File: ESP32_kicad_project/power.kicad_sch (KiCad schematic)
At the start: 24 parts, among them J2 USB_C_Receptacle_USB2.0_16P, Q1 AO3401A, U1 TPS56339DDC

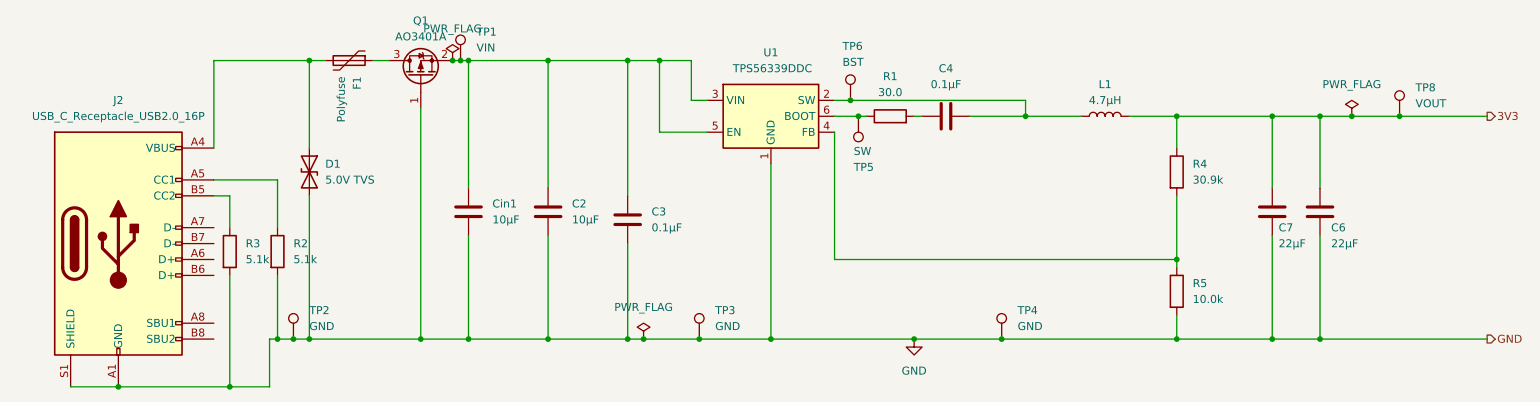
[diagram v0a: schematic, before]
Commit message: added USB chip, implemented ESP32 auto reset DTR RTS circuit
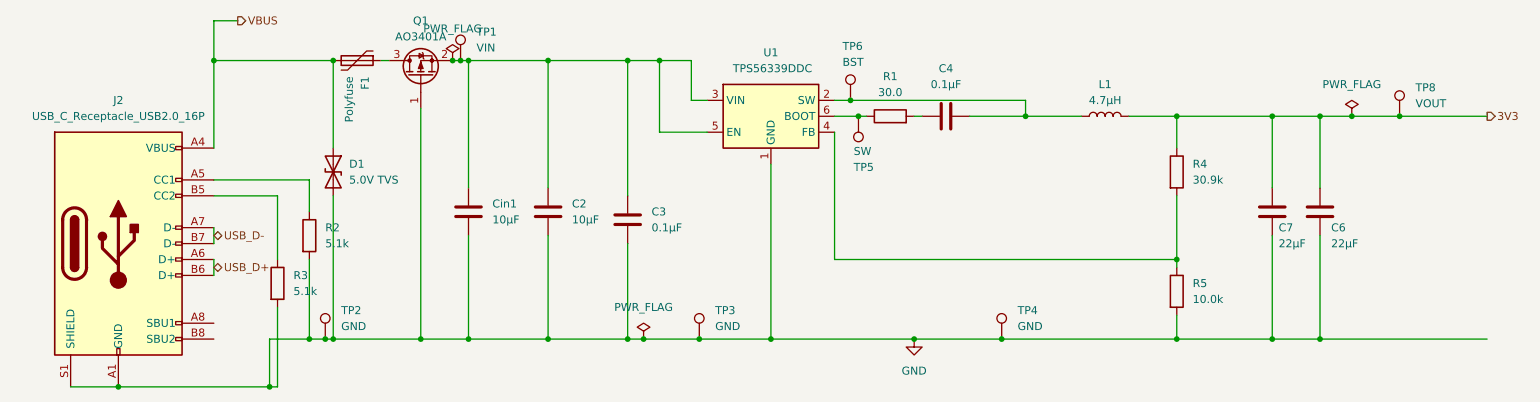
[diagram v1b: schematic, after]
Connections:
- net VBUS: now reaches D1.1 (A1), F1.2, J2.A4 (VBUS), J2.A9 (VBUS), J2.B4 (VBUS), J2.B9 (VBUS)
- net USB_D+: now reaches J2.A6 (D+)
- net USB_D+: now also J2.B6 (D+)
- net USB_D-: now reaches J2.A7 (D-)
- net USB_D-: now also J2.B7 (D-)
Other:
- moved on the sheet: D1, F1, R2, R3, TP2

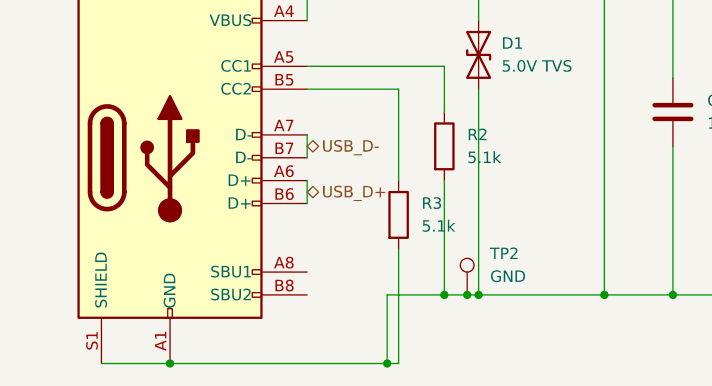
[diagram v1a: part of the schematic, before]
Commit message: completed USB-UART, created GPIO pin connectors, completed schematic work. moving on to PCB
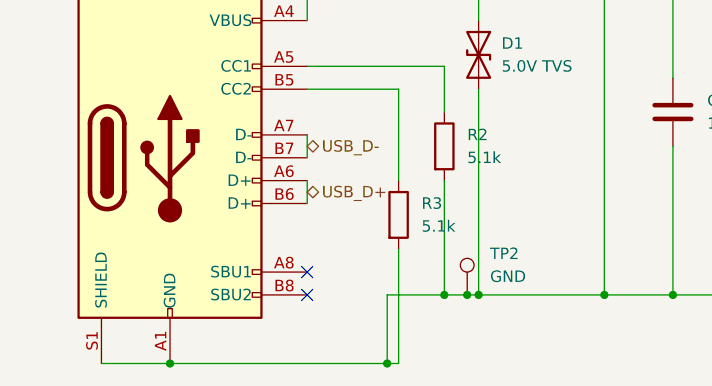
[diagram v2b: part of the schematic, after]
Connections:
- no-connect marks 0 -> 2
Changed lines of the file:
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@@
 		(color 0 0 0 0)
+	)
+	(no_connect
+		(at 58.42 118.11)
+	)
+	(no_connect
+		(at 58.42 115.57)
 	)
 	(wire

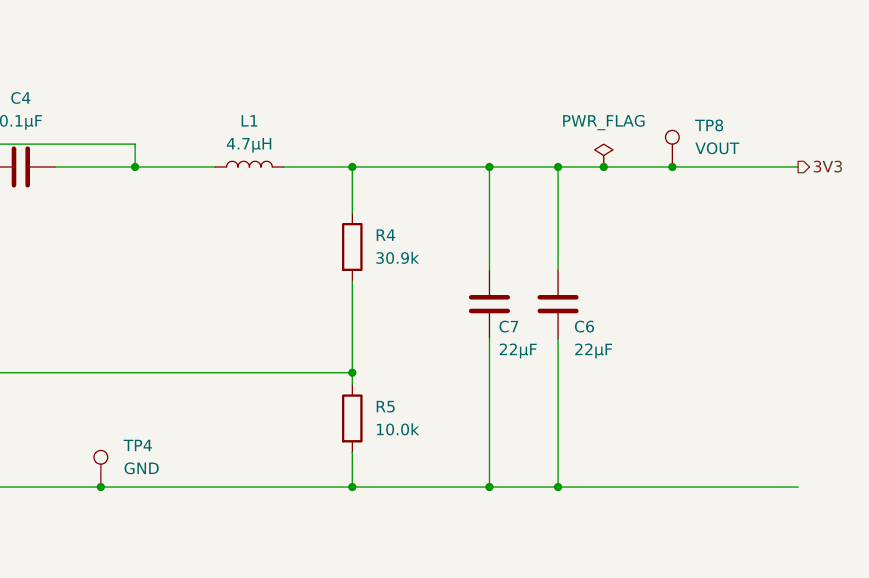
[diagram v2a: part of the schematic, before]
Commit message: completed schematic design, replaced regulator output inductor with a smaller part, fit components in a board in PCB editor, will start routing
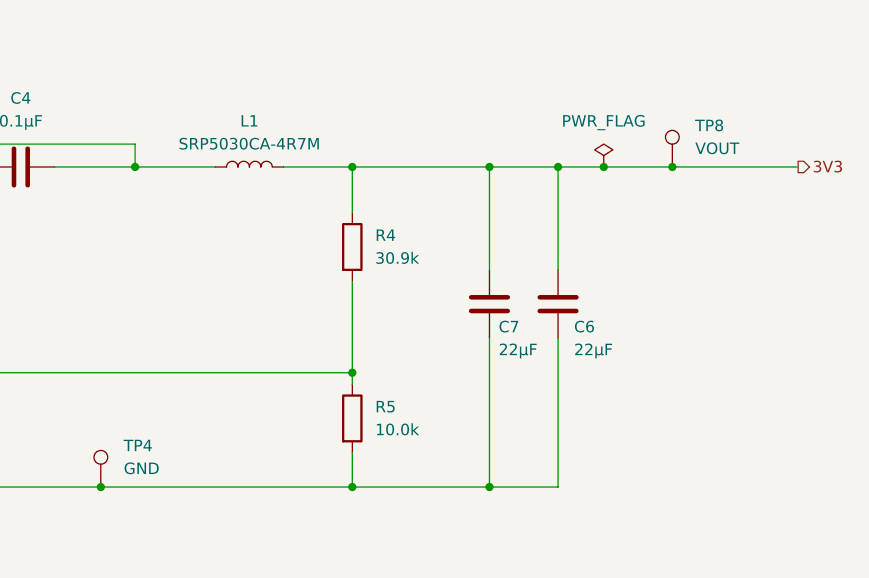
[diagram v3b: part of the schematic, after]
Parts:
- L1: value 4.7µH -> SRP5030CA-4R7M; footprint personal_library:Inductor_SDS74M-4R7M-LF -> Inductor_SMD:L_Bourns_SRP5030T
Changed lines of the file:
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@@
-	)
-	(junction
-		(at 234.95 118.11)
-		(diameter 0)
-		(color 0 0 0 0)
 	)
 	(junction
@@
 		(pts
 			(xy 58.42 67.31) (xy 58.42 73.66)
-		)
-		(stroke
-			(width 0)
-			(type default)
-		)
-	)
-	(wire
-		(pts
-			(xy 234.95 118.11) (xy 261.62 118.11)
 		)
 		(stroke
@@
 			)
 		)
-		(property "Value" "4.7µH"
+		(property "Value" "SRP5030CA-4R7M"
 			(at 200.66 80.01 90)
 			(effects
@@
 			)
 		)
-		(property "Footprint" "personal_library:Inductor_SDS74M-4R7M-LF"
+		(property "Footprint" "Inductor_SMD:L_Bourns_SRP5030T"
 			(at 200.66 82.55 0)
 			(effects

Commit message: routed the regulator properly, VBUS and 3V3 are also routed
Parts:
- L1: MPN (none) -> SRP5030CA-4R7M
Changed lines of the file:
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@@
+			)
+		)
+		(property "MPN" "SRP5030CA-4R7M"
+			(at 200.66 82.55 90)
+			(effects
+				(font
+					(size 1.27 1.27)
+				)
+				(hide yes)
 			)
 		)
